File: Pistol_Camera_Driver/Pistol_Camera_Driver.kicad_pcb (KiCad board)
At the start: 2 copper layers, 95.8 x 38.7 mm, 55 parts, among them J1 Screw_Terminal_01x02, J2 Objective, J3 Screw_Terminal_01x02, J4 Screw_Terminal_01x02, J5 SONAR, J6 Joystick, J7 Screw_Terminal_01x02, J8 Screw_Terminal_01x04, J9 Screw_Terminal_01x02, U1 LM7805_TO220, U10 RS0101YH6, U11 LDD-700L, U2 LM317_TO-263, U3 Raspberri_Pi_Pico, U4 DRV8834PWP, U5 DRV8834PWP, U6 RS0101YH6, U7 LDD-700L, U8 RS0101YH6, U9 LDD-700L

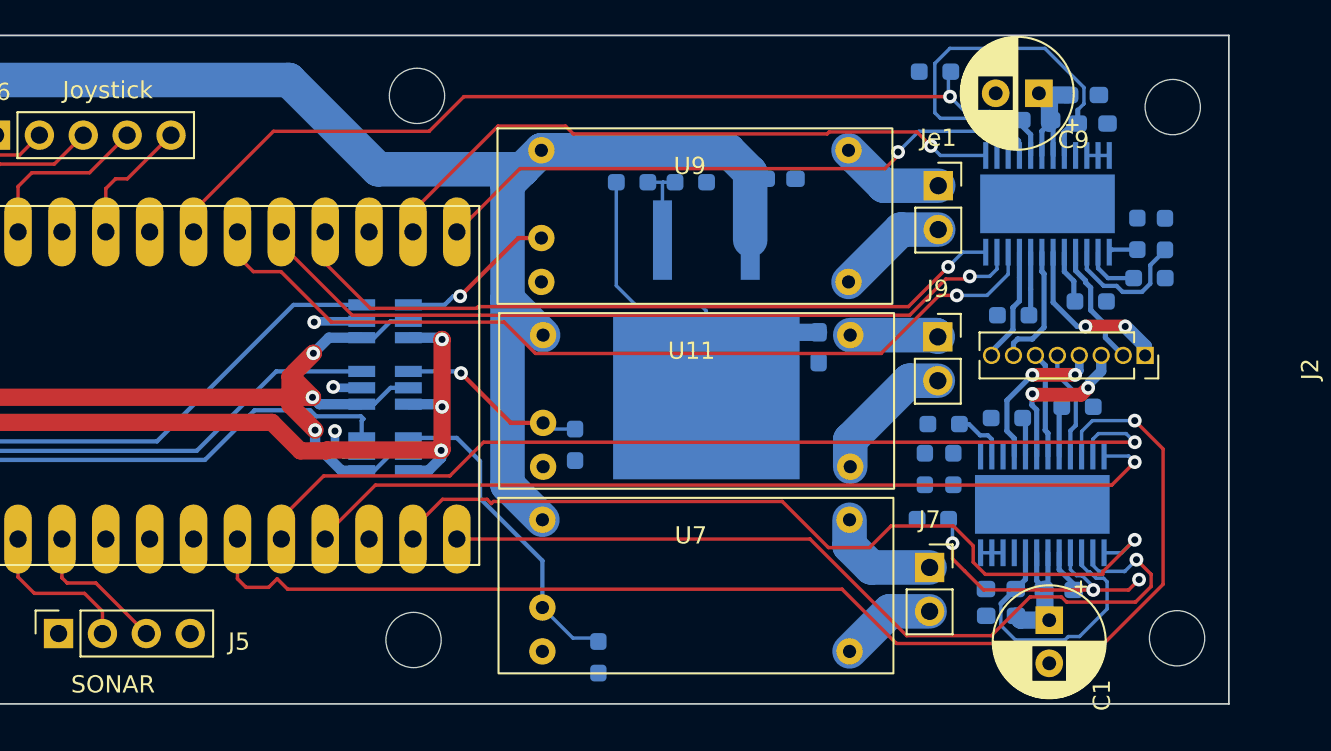
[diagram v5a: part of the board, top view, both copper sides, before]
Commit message: v1.2 The second routing iteration
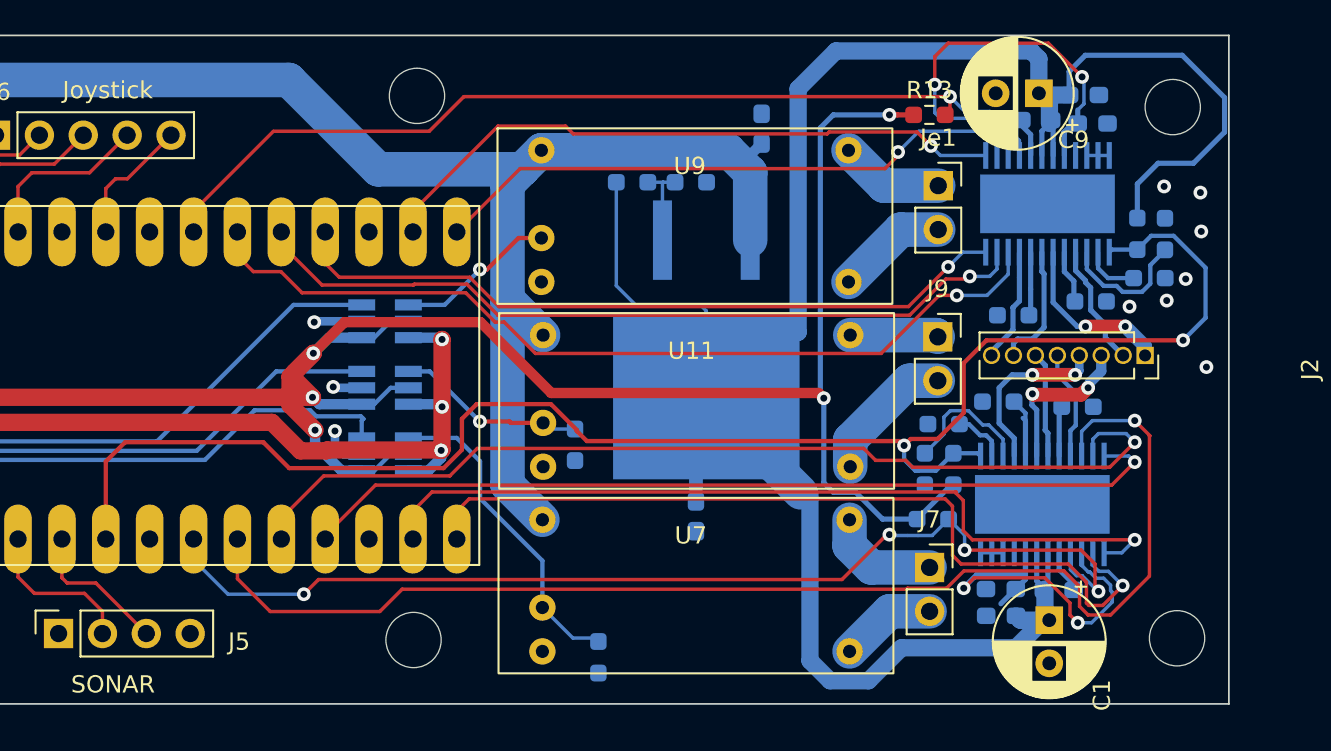
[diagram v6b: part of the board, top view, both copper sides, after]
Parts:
- R13: moved to F.Cu
- moved C6 12.1 mm to (141.6, 52.2)
- moved C4 3.10 mm to (145.3, 29.8), turned to 90 degrees
- moved R13 2.52 mm to (155.1, 28.9)
- moved R5 1.07 mm to (159.1, 45.5)
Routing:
- net MOTORS_nSLEEP: track 1.69 -> 93.2 mm, vias 0 -> 2
- net +3.3VP: track 47.0 -> 138.4 mm
- net +3V3: track 93.9 -> 161.6 mm, vias 3 -> 5
- net nFLT1: track 17.1 -> 62.4 mm, vias 3 -> 4
- net Net-(R4-Pad2): track 0.00 -> 7.78 mm
- net Net-(C8-Pad1): track 17.0 -> 24.1 mm, vias 0 -> 2
- net +12V: track 88.4 -> 90.4 mm
- net M0_1: track 49.6 -> 48.2 mm
- net Net-(R5-Pad2): track 2.27 -> 3.65 mm
- net AOUT1_1: track 9.22 -> 10.3 mm
- net STEP1: track 56.2 -> 57.1 mm
- net Net-(C12-Pad1): track 23.2 -> 24.0 mm, vias 0 -> 2
- net M1_1: track 49.6 -> 49.0 mm
- net nEN1: track 74.2 -> 73.6 mm
- net GND: vias 3 -> 10

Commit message: v1.3 seems 2B ready
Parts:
- moved R16 3.87 mm to (133.2, 44.4), turned to 90 degrees
- moved R15 2.84 mm to (135.4, 57.5), turned to 0 degrees
- moved REF** 0.60 mm to (125.3, 28.4)
- moved J1 0.51 mm to (87.2, 58.9)
- moved C5 0.45 mm to (159.2, 58.4)
- moved C10 0.35 mm to (164.1, 27.4)
- moved R2 0.29 mm to (155.6, 47.0)
- moved C12 0.14 mm to (164.6, 29.4)
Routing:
- net +12V: track 90.4 -> 107.9 mm
- net +5V: track 72.8 -> 86.6 mm
- net GND: track 12.5 -> 24.7 mm, vias 10 -> 193
- net DIR1: track 50.8 -> 58.6 mm
- net STEP1: track 57.1 -> 61.8 mm
- net DIR2: track 42.4 -> 46.6 mm
- net STEP2: track 46.0 -> 49.6 mm
- net M0_1: track 48.2 -> 51.7 mm
- net Net-(R16-Pad1): track 11.0 -> 14.1 mm
- net nEN2: track 51.5 -> 53.7 mm
- net M1_2: track 35.0 -> 36.5 mm
- net nFLT1: track 62.4 -> 63.6 mm
- net Net-(C12-Pad1): track 24.0 -> 23.1 mm
- net Net-(U8-Pad4): track 9.31 -> 10.0 mm, vias 1 -> 0
- net nFLT2: track 55.0 -> 55.5 mm
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- added copper zone on B.Cu, net GND
- added copper zone on F.Cu, net GND

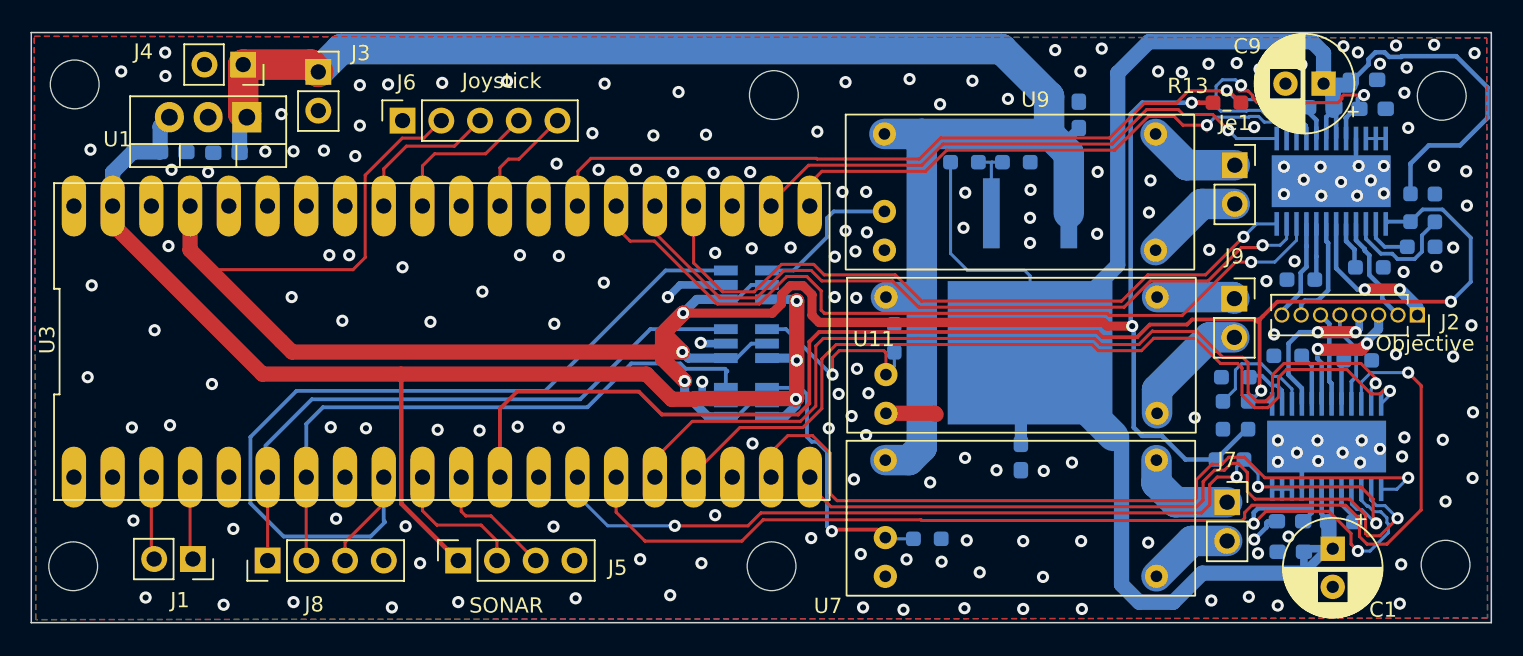
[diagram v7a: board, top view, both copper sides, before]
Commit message: v1.4 Bluetooth was added, mounting holes were corrected. Seems 2B ready!
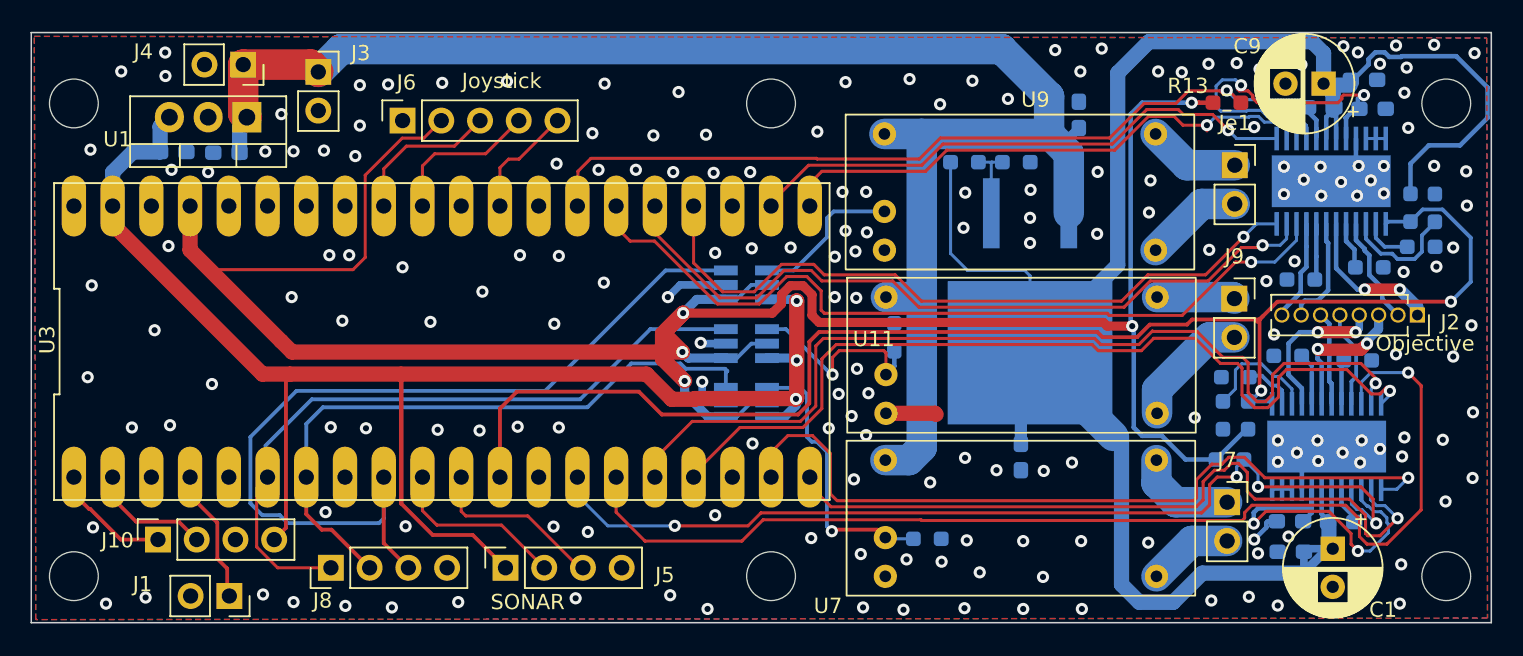
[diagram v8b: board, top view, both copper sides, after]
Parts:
- removed R16: R, Resistor_SMD:R_0603_1608Metric_Pad0.98x0.95mm_HandSolder
- added J10: Bluetooth, Connector_PinSocket_2.54mm:PinSocket_1x04_P2.54mm_Vertical, F.Cu at (85.0, 57.6)
- added R15: R, Resistor_SMD:R_0603_1608Metric_Pad0.98x0.95mm_HandSolder, B.Cu at (133.2, 44.3)
- moved J8 4.18 mm to (96.3, 59.5)
- moved J1 3.40 mm to (89.6, 61.3)
- moved J5 3.14 mm to (107.8, 59.5)
- moved REF** 1.25 mm to (79.4, 29.0)
- moved REF** 0.75 mm to (169.4, 60.0)
- moved REF** 0.65 mm to (79.4, 60.0)
- moved REF** 0.65 mm to (125.2, 60.0)
- moved REF** 0.58 mm to (169.4, 29.0)
- moved REF** 0.58 mm to (125.2, 29.0)
- renumbered R11 to R10, R12 to R11, R14 to R12, R15 to R14, R8 to R7, R7 to R8, R10 to R9
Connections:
- U3 pad 1: unconnected-(U3-Pad1) -> RX
- U3 pad 2: unconnected-(U3-Pad2) -> TX
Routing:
- net +5V: track 86.6 -> 101.2 mm
- net TX: track 0.00 -> 8.02 mm
- net RX: track 0.00 -> 7.85 mm
- net GND: track 24.7 -> 19.2 mm
- net PWM_RED: track 39.1 -> 44.0 mm
- net ECHO: track 8.46 -> 11.8 mm
- net Strobe Input: track 5.43 -> 8.53 mm
- net PWM_UV: track 39.6 -> 42.1 mm
- net TRIG: track 9.19 -> 11.7 mm
- net PWM_WHITE: track 59.7 -> 60.5 mm
